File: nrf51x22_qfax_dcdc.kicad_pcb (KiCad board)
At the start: 2 copper layers, 14.8 x 16.4 mm, 46 parts, among them U1 nrf51822-qfax, X1 Crystal-4, X2 32.768kHz

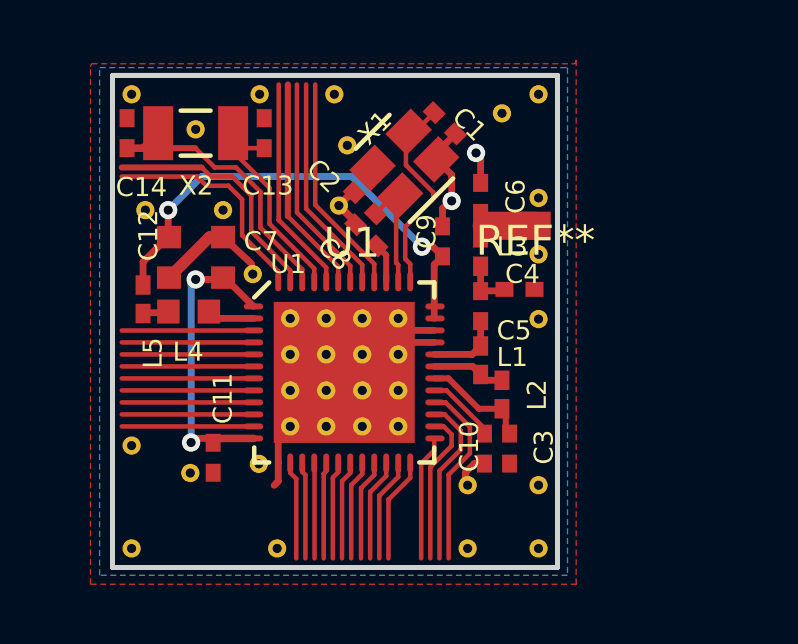
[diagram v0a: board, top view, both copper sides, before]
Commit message: converted qfaa dcdc reference layout .9
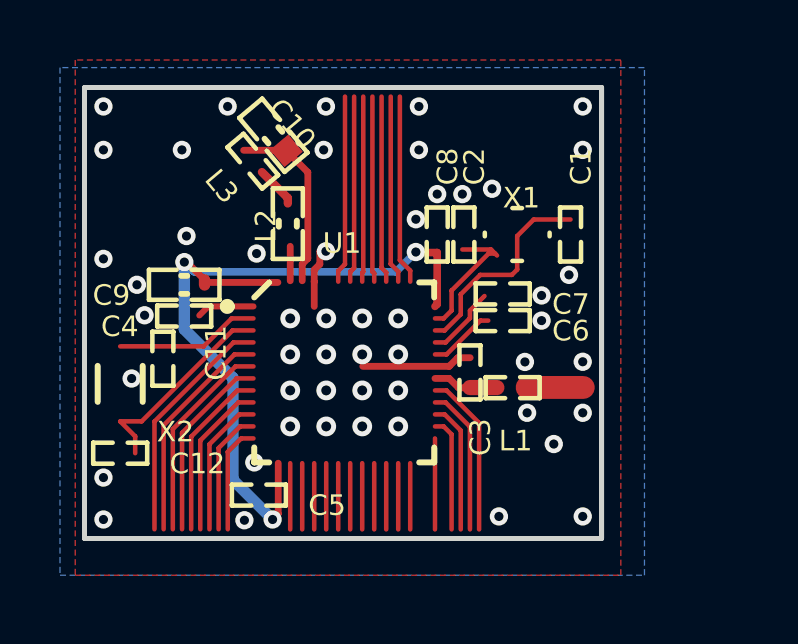
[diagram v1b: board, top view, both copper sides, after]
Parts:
- removed C1, C13, C14: 12pF, dcdc:CAPC1005X04L
- removed C10: 47nF, dcdc:CAPC1005X04L
- removed the C11 at (79.7, -82.6)
- removed the C12 at (78.3, -89.3)
- removed C3: 2.2nF, dcdc:CAPC1005X04L
- removed C4: 1.0pF, dcdc:CAPC1005X04L
- removed L1: 4.7nH, dcdc:INDC1005X04L
- removed L3: 3.3nH, dcdc:INDC1005X04L
- removed L4: 10uH, dcdc:INDC1608X06L
- removed REF** (x23): VIA-0.6096, dcdc:VIA-0.6096
- removed REF**: antenna, dcdc:antenna
- added C11: Chip Capacitor, 2-Leads, Body 1.6x0.8mm, IPC High Density, CAPC1608X06L, F.Cu at (81.7, -93.4)
- added C11: Chip Capacitor, 2-Leads, Body 1.0x0.5mm, IPC High Density, CAPC1005X04L, F.Cu at (89.4, -88.1)
- added C11: Chip Capacitor, 2-Leads, Body 1.0x0.5mm, IPC High Density, CAPC1005X04L, F.Cu at (78.1, -85.9)
- added C12: Chip Capacitor, 2-Leads, Body 1.0x0.5mm, IPC High Density, CAPC1005X04L, F.Cu at (87.2, -90.1)
- added C12: Chip Capacitor, 2-Leads, Body 1.0x0.5mm, IPC High Density, CAPC1005X04L, F.Cu at (76.6, -82.8)
- added C20: Chip Capacitor, 2-Leads, Body 1.0x0.5mm, IPC High Density, CAPC1005X04L, F.Cu at (88.3, -85.5)
- added L6: Chip Inductor, 2-Leads, Body 1.0x0.5mm, IPC High Density, INDC1005X04L, F.Cu at (81.1, -92.5)
- C2: value 12pF -> Chip Capacitor, 2-Leads, Body 1.0x0.5mm, IPC High Density; footprint dcdc:CAPC1005X04L -> CAPC1005X04L
- C5: value 3.9pF -> Chip Capacitor, 2-Leads, Body 1.0x0.5mm, IPC High Density; footprint dcdc:CAPC1005X04L -> CAPC1005X04L
- C6: value 1.5pF -> Chip Capacitor, 2-Leads, Body 1.0x0.5mm, IPC High Density; footprint dcdc:CAPC1005X04L -> CAPC1005X04L
- C7: value 4.7uF -> Chip Capacitor, 2-Leads, Body 1.0x0.5mm, IPC High Density; footprint dcdc:CAPC1608X06L -> CAPC1005X04L
- C8: value 100nF -> Chip Capacitor, 2-Leads, Body 1.0x0.5mm, IPC High Density; footprint dcdc:CAPC1005X04L -> CAPC1005X04L
- C9: value 1.0nF -> Chip Capacitor, 2-Leads, Body 1.6x0.8mm, IPC High Density; footprint dcdc:CAPC1005X04L -> CAPC1608X06L
- L2: value 27nH -> Chip Inductor, 2-Leads, Body 1.0x0.5mm, IPC High Density; footprint dcdc:INDC1005X04L -> INDC1005X04L
- L5: value 15nH -> Chip Inductor, 2-Leads, Body 1.6x0.8mm, IPC High Density; footprint dcdc:INDC1005X04L -> INDC1608X06L
- U1: value nrf51822-qfax -> QFN, 48-Leads, Body 6,0x6,0mm (max), Pitch 0,40mm, IPC Medium Density; footprint nrf:nrf51-qfax-1ep-vias -> QFN40P600X600X90-48N
- X1: value Crystal-4 -> Crystal 2.0 x 1.6 mm; footprint dcdc:BT-XTAL_2520 -> BT-XTAL_2016
- X2: value 32.768kHz -> XTAL SMD 3.2 x 1.5 mm; footprint dcdc:XTAL_3215 -> XTAL_3215
- moved C6 12.4 mm to (81.3, -81.4), turned to 0 degrees
- moved C7 11.6 mm to (91.6, -90.1)
- moved C5 9.89 mm to (78.8, -87.4), turned to 0 degrees
- moved C9 8.73 mm to (78.8, -88.4), turned to 0 degrees
- moved X2 8.73 mm to (76.6, -85.1), turned to 0 degrees
- moved L5 5.44 mm to (82.2, -90.4)
- moved C8 5.36 mm to (89.4, -87.2), turned to 0 degrees
- moved X1 4.44 mm to (89.9, -90.1), turned to 0 degrees
- moved C2 3.46 mm to (88.1, -90.1), turned to 0 degrees
- moved L2 0.42 mm to (89.7, -85.0)
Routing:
- net Net1: track 0.00 -> 302.1 mm
- net (no net): track 149.8 -> 0.00 mm
- net GND: track 19.3 -> 0.00 mm, vias 2 -> 51
- net Net-(C12-Pad1): track 15.7 -> 0.00 mm, vias 2 -> 0
- net Net-(C11-Pad1): track 11.2 -> 0.00 mm, vias 2 -> 0
- net Net-(C14-Pad2): track 9.89 -> 0.00 mm
- net Net-(C1-Pad1): track 6.86 -> 0.00 mm
- net Net-(C13-Pad2): track 6.04 -> 0.00 mm
- net Net-(C2-Pad1): track 4.00 -> 0.00 mm
- net Net-(C3-Pad1): track 3.56 -> 0.00 mm
- net Net-(C5-Pad2): track 2.52 -> 0.00 mm
- net Net-(L1-Pad2): track 2.45 -> 0.00 mm
- net Net-(C10-Pad2): track 2.37 -> 0.00 mm
- net Net-(C4-Pad1): track 1.69 -> 0.00 mm
- net Net-(C6-Pad1): track 1.63 -> 0.00 mm
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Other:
- board size 14.8 x 16.4 mm -> 17.2 x 15 mm
- net class Default: clearance 0.1524 -> 0.152400; trace_width 0.254 -> 0.254000; via_dia 0.6096 -> 0.889; via_drill 0.3048 -> 0.635
- net class Net-(C6-Pad1) removed
- rule trace_clearance: 0.1524 -> 0.127
- rule trace_min: 0.152 -> 0.254
- rule via_min_drill: 0.3048 -> 0.508
- rule via_min_size: 0.6096 -> 0.889
- board text removed: "C13"
- board text removed: "C14"
- board text removed: "L4"
- board text removed: "L5"

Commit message: kicad touches and updats kicad_pcb
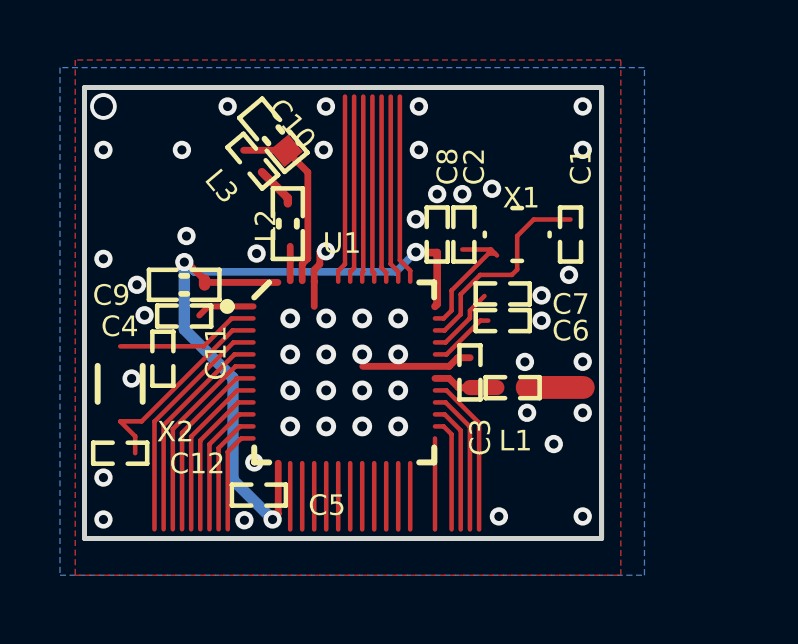
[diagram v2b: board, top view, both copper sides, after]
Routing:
- net Net1: track 302.1 -> 0.00 mm
- net (no net): track 0.00 -> 296.0 mm, vias 0 -> 54
- net DEC4: track 0.00 -> 6.11 mm
- net VDD_NRF: vias 3 -> 0
- net GND: vias 51 -> 0
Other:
- net class Default: clearance 0.152400 -> 0.1524; trace_width 0.254000 -> 0.254
- rule trace_clearance: 0.127 -> 0.1524

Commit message: swap for stiched vias
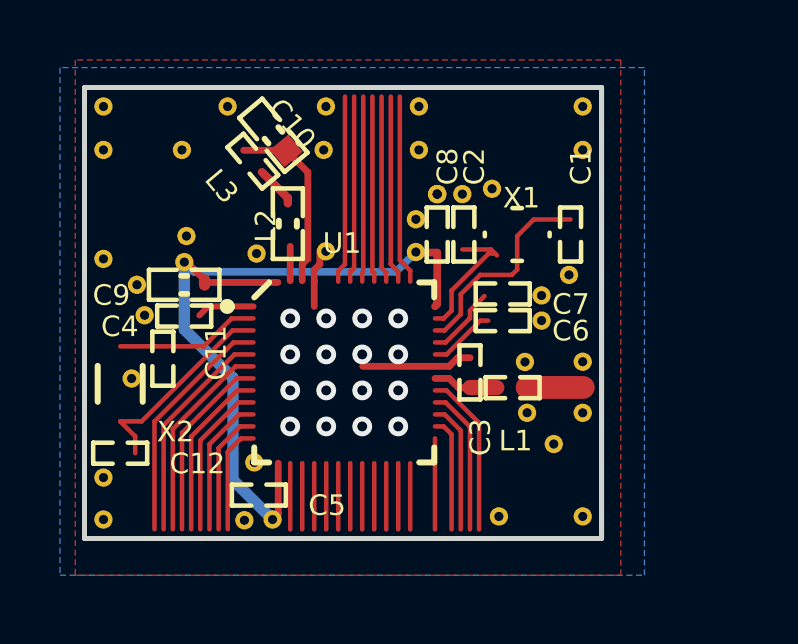
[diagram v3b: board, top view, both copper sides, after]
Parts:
- added REF**: VIA-0.6096, dcdc:VIA-0.6096, F.Cu at (92.1, -94.4)
- added REF**: VIA-0.6096, dcdc:VIA-0.6096, F.Cu at (92.1, -80.7)
- added REF**: VIA-0.6096, dcdc:VIA-0.6096, F.Cu at (89.3, -80.7)
- added REF**: VIA-0.6096, dcdc:VIA-0.6096, F.Cu at (92.1, -84.1)
- added REF**: VIA-0.6096, dcdc:VIA-0.6096, F.Cu at (90.2, -84.1)
- added REF**: VIA-0.6096, dcdc:VIA-0.6096, F.Cu at (92.1, -85.8)
- added REF**: VIA-0.6096, dcdc:VIA-0.6096, F.Cu at (91.6, -88.7)
- added REF**: VIA-0.6096, dcdc:VIA-0.6096, F.Cu at (89.0, -91.6)
- added REF**: VIA-0.6096, dcdc:VIA-0.6096, F.Cu at (92.1, -92.9)
- added REF**: VIA-0.6096, dcdc:VIA-0.6096, F.Cu at (86.5, -90.6)
- added REF**: VIA-0.6096, dcdc:VIA-0.6096, F.Cu at (88.0, -91.4)
- added REF**: VIA-0.6096, dcdc:VIA-0.6096, F.Cu at (86.6, -94.4)
- added REF** (x2): VIA-0.6096, dcdc:VIA-0.6096, F.Cu at (87.2, -91.4)
- added REF**: VIA-0.6096, dcdc:VIA-0.6096, F.Cu at (86.6, -92.9)
- added REF**: VIA-0.6096, dcdc:VIA-0.6096, F.Cu at (83.4, -92.9)
- added REF**: VIA-0.6096, dcdc:VIA-0.6096, F.Cu at (76.1, -89.3)
- added REF**: VIA-0.6096, dcdc:VIA-0.6096, F.Cu at (78.8, -90.0)
- added REF**: VIA-0.6096, dcdc:VIA-0.6096, F.Cu at (76.1, -92.9)
- added REF**: VIA-0.6096, dcdc:VIA-0.6096, F.Cu at (78.8, -89.2)
- added REF**: VIA-0.6096, dcdc:VIA-0.6096, F.Cu at (77.2, -88.4)
- added REF**: VIA-0.6096, dcdc:VIA-0.6096, F.Cu at (86.5, -89.5)
- added REF**: VIA-0.6096, dcdc:VIA-0.6096, F.Cu at (81.2, -89.5)
- added REF**: VIA-0.6096, dcdc:VIA-0.6096, F.Cu at (80.8, -80.6)
- added REF**: VIA-0.6096, dcdc:VIA-0.6096, F.Cu at (91.1, -83.1)
- added REF**: VIA-0.6096, dcdc:VIA-0.6096, F.Cu at (81.7, -80.6)
- added REF**: VIA-0.6096, dcdc:VIA-0.6096, F.Cu at (81.1, -82.5)
- added REF**: VIA-0.6096, dcdc:VIA-0.6096, F.Cu at (77.5, -87.4)
- added REF**: VIA-0.6096, dcdc:VIA-0.6096, F.Cu at (90.7, -87.2)
- added REF**: VIA-0.6096, dcdc:VIA-0.6096, F.Cu at (90.7, -88.1)
- added REF**: VIA-0.6096, dcdc:VIA-0.6096, F.Cu at (78.7, -92.9)
- added REF**: VIA-0.6096, dcdc:VIA-0.6096, F.Cu at (90.1, -85.8)
- added REF**: VIA-0.6096, dcdc:VIA-0.6096, F.Cu at (83.5, -89.5)
- added REF**: VIA-0.6096, dcdc:VIA-0.6096, F.Cu at (76.1, -94.4)
- added REF**: VIA-0.6096, dcdc:VIA-0.6096, F.Cu at (80.2, -94.4)
- added REF**: VIA-0.6096, dcdc:VIA-0.6096, F.Cu at (83.5, -94.4)
- added REF**: VIA-0.6096, dcdc:VIA-0.6096, F.Cu at (77.0, -85.3)
- added REF**: VIA-0.6096, dcdc:VIA-0.6096, F.Cu at (76.1, -82.0)
- added REF**: VIA-0.6096, dcdc:VIA-0.6096, F.Cu at (76.1, -80.6)
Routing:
- net GND: track 0.00 -> 28.0 mm
- net (no net): track 296.0 -> 268.0 mm, vias 54 -> 16

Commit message: replace components with library parts
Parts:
- removed the C11 at (81.7, -93.4)
- removed the C11 at (89.4, -88.1)
- removed the C11 at (78.1, -85.9)
- removed the C12 at (87.2, -90.1)
- removed the C12 at (76.6, -82.8)
- removed C20: Chip Capacitor, 2-Leads, Body 1.0x0.5mm, IPC High Density, CAPC1005X04L
- removed L5: Chip Inductor, 2-Leads, Body 1.6x0.8mm, IPC High Density, INDC1608X06L
- removed L6: Chip Inductor, 2-Leads, Body 1.0x0.5mm, IPC High Density, INDC1005X04L
- removed the REF** at (87.2, -91.4) (x2)
- added C1: Chip Capacitor, 2-Leads, Body 1.0x0.5mm, IPC High Density, dcdc:CAPC1005X04L, F.Cu at (91.6, -90.1)
- added C10: Chip Capacitor, 2-Leads, Body 1.6x0.8mm, IPC High Density, dcdc:CAPC1608X06L, F.Cu at (81.7, -93.4)
- added C11: Chip Capacitor, 2-Leads, Body 1.0x0.5mm, IPC High Density, dcdc:CAPC1005X04L, F.Cu at (78.1, -85.9)
- added C12: Chip Capacitor, 2-Leads, Body 1.0x0.5mm, IPC High Density, dcdc:CAPC1005X04L, F.Cu at (76.6, -82.8)
- added C3: Chip Capacitor, 2-Leads, Body 1.0x0.5mm, IPC High Density, dcdc:CAPC1005X04L, F.Cu at (88.3, -85.5)
- added C4: Chip Capacitor, 2-Leads, Body 1.0x0.5mm, IPC High Density, dcdc:CAPC1005X04L, F.Cu at (78.8, -87.4)
- added L1: Chip Inductor, 2-Leads, Body 1.0x0.5mm, IPC High Density, dcdc:INDC1005X04L, F.Cu at (89.7, -85.0)
- added L3: Chip Inductor, 2-Leads, Body 1.0x0.5mm, IPC High Density, dcdc:INDC1005X04L, F.Cu at (81.1, -92.5)
- added REF** (x2): VIA-0.6096, dcdc:VIA-0.6096, F.Cu at (87.2, -91.4)
- C2, C5, C6, C7, C8: footprint CAPC1005X04L -> dcdc:CAPC1005X04L
- C9: footprint CAPC1608X06L -> dcdc:CAPC1608X06L
- L2: value Chip Inductor, 2-Leads, Body 1.0x0.5mm, IPC High Density -> Chip Inductor, 2-Leads, Body 1.6x0.8mm, IPC High Density; footprint INDC1005X04L -> dcdc:INDC1608X06L
- U1: footprint QFN40P600X600X90-48N -> nrf:nrf51-qfax-1ep-vias
- X2: footprint XTAL_3215 -> dcdc:XTAL_3215
- moved C6 9.99 mm to (89.4, -87.2)
- moved L2 9.27 mm to (82.2, -90.4), turned to 90 degrees
- moved C5 6.47 mm to (81.3, -81.4)
- moved C8 3.61 mm to (87.2, -90.1), turned to 90 degrees
- moved C7 3.01 mm to (89.4, -88.1)
- turned C2 to 90 degrees
- turned C9 to 90 degrees
- turned X2 to 90 degrees
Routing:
- net (no net): track 268.0 -> 274.1 mm, vias 16 -> 0
- net DEC4: track 6.11 -> 0.00 mm

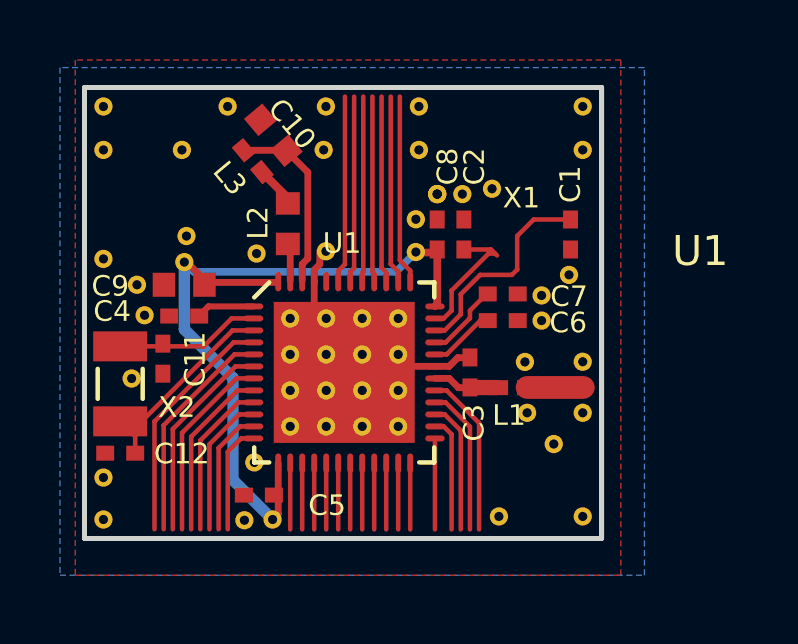
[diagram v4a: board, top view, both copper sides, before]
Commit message: fix zones and pour
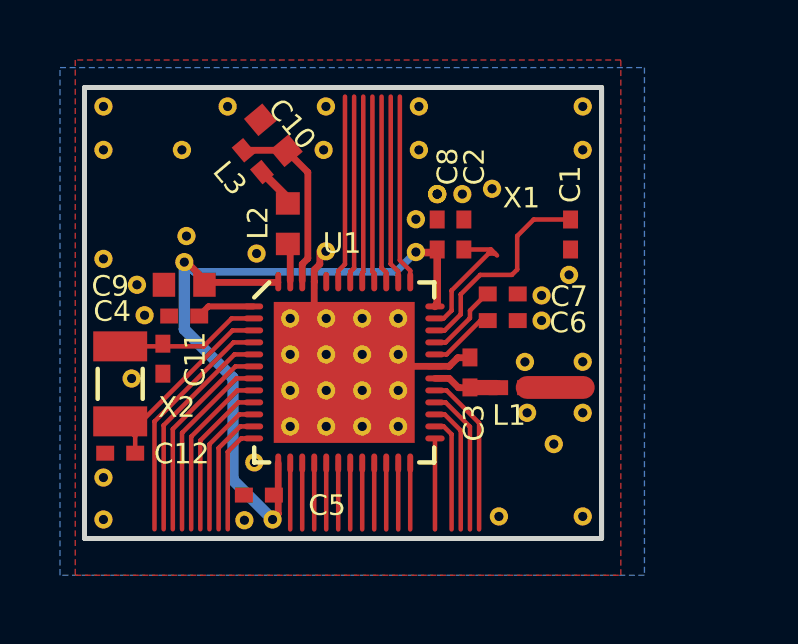
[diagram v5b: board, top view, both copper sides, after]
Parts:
- removed the REF** at (87.2, -91.4) (x2)
- added REF** (x2): VIA-0.6096, dcdc:VIA-0.6096, F.Cu at (87.2, -91.4)
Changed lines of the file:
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@@
   (general
     (links 38)
-    (no_connects 35)
+    (no_connects 0)
     (area 40.900936 -125.826416 125.126534 -49.754218)
     (thickness 1.6)
@@
     (last_trace_width 0.254)
     (trace_clearance 0.1524)
-    (zone_clearance 0.0144)
-    (zone_45_only no)
+    (zone_clearance 0.09144)
+    (zone_45_only yes)
     (trace_min 0.254)
     (segment_width 0.2)
@@
     (tags "QFN 0.4")
     (attr smd)
-    (fp_text reference U1 (at 11.867965 -4.043383) (layer F.SilkS)
+    (fp_text reference U1 (at 11.867965 -4.043383) (layer F.SilkS) hide
       (effects (font (size 1 1) (thickness 0.15)))
     )
@@
   (zone (net 2) (net_name GND) (layer F.Cu) (hatch edge 0.508)
     (priority 100)
-    (connect_pads thru_hole_only (clearance 0.09144))
+    (connect_pads (clearance 0.09144))
     (min_thickness 0.254)
-    (fill (mode segment) (arc_segments 32) (thermal_gap 0.254) (thermal_bridge_width 0.254))
+    (fill yes (arc_segments 32) (thermal_gap 0.254) (thermal_bridge_width 0.255))
     (polygon
       (pts
@@
   (zone (net 2) (net_name GND) (layer B.Cu) (hatch edge 0.508)
     (priority 99)
-    (connect_pads thru_hole_only (clearance 0.09144))
+    (connect_pads (clearance 0.09144))
     (min_thickness 0.254)
-    (fill (mode segment) (arc_segments 32) (thermal_gap 0.254) (thermal_bridge_width 0.254))
+    (fill yes (arc_segments 32) (thermal_gap 0.254) (thermal_bridge_width 0.255))
     (polygon
       (pts
-        (xy 74.631735 -95.651625) (xy 74.631735 -78.730462) (xy 94.113535 -78.730462) (xy 94.113535 -95.651625) (xy 74.631735 -95.651625)
+        (xy 94.113535 -78.730462) (xy 74.631735 -78.730462) (xy 74.631735 -95.651625) (xy 94.113535 -95.651625) (xy 94.113535 -78.730462)
       )
     )
+  )
+  (zone (net 0) (net_name "") (layer F.Cu) (hatch edge 0.508)
+    (connect_pads (clearance 0.09144))
+    (min_thickness 0.254)
+    (keepout (tracks allowed) (vias allowed) (copperpour not_allowed))
+    (fill (arc_segments 32) (thermal_gap 0.254) (thermal_bridge_width 0.255))
+    (polygon
+      (pts
+        (xy 89.7763 -83.7692) (xy 88.265 -83.7692) (xy 88.265 -86.6775) (xy 89.7763 -86.6775) (xy 89.7763 -83.7692)
+      )
+    )

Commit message: cleanup
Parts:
- removed the REF** at (87.2, -91.4) (x2)
- added REF** (x2): VIA-0.6096, dcdc:VIA-0.6096, F.Cu at (87.2, -91.4)

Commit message: schematic and netlist imported to board
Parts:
- removed the REF** at (87.2, -91.4) (x2)
- added REF** (x2): VIA-0.6096, dcdc:VIA-0.6096, F.Cu at (87.2, -91.4)
- C1, C11, C12, C2: value Chip Capacitor, 2-Leads, Body 1.0x0.5mm, IPC High Density -> 12pF
- C10: value Chip Capacitor, 2-Leads, Body 1.6x0.8mm, IPC High Density -> 1.0uF
- C3: value Chip Capacitor, 2-Leads, Body 1.0x0.5mm, IPC High Density -> .8pF
- C4, C5, C8: value Chip Capacitor, 2-Leads, Body 1.0x0.5mm, IPC High Density -> 100nF
- C6: value Chip Capacitor, 2-Leads, Body 1.0x0.5mm, IPC High Density -> NC
- C7: value Chip Capacitor, 2-Leads, Body 1.0x0.5mm, IPC High Density -> 100pF
- C9: value Chip Capacitor, 2-Leads, Body 1.6x0.8mm, IPC High Density -> 4.7uF
- L1: value Chip Inductor, 2-Leads, Body 1.0x0.5mm, IPC High Density -> 3.9nH
- L2: value Chip Inductor, 2-Leads, Body 1.6x0.8mm, IPC High Density -> 10uH
- L3: value Chip Inductor, 2-Leads, Body 1.0x0.5mm, IPC High Density -> 15nH
- U1: value QFN, 48-Leads, Body 6,0x6,0mm (max), Pitch 0,40mm, IPC Medium Density -> nrf51822-qfax
- X1: value Crystal 2.0 x 1.6 mm -> Crystal-4
- X2: value XTAL SMD 3.2 x 1.5 mm -> 32.768kHz
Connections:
- C1 pad 1: (no net) -> Net-(C1-Pad1)
- C1 pad 2: (no net) -> GND
- C10 pad 1: (no net) -> GND
- C10 pad 2: DEC4 -> Net-(C10-Pad2)
- C11 pad 1: (no net) -> GND
- C11 pad 2: (no net) -> Net-(C11-Pad2)
- C12 pad 1: (no net) -> GND
- C12 pad 2: (no net) -> Net-(C12-Pad2)
- C2 pad 1: (no net) -> Net-(C2-Pad1)
- C2 pad 2: (no net) -> GND
- C3 pad 1: (no net) -> Net-(C3-Pad1)
- C3 pad 2: (no net) -> GND
- C4 pad 1: (no net) -> GND
- C4 pad 2: (no net) -> Net-(C4-Pad2)
- C5 pad 1: (no net) -> GND
- C5 pad 2: (no net) -> /VDD_nRF
- C6 pad 1: (no net) -> GND
- C6 pad 2: (no net) -> Net-(C6-Pad2)
- C7 pad 1: (no net) -> GND
- C7 pad 2: (no net) -> Net-(C7-Pad2)
- C8 pad 1: (no net) -> GND
- C8 pad 2: (no net) -> /VDD_nRF
- C9 pad 1: (no net) -> GND
- C9 pad 2: (no net) -> /VDD_nRF
- L1 pad 1: (no net) -> Net-(C3-Pad1)
- L2 pad 1: (no net) -> Net-(L2-Pad1)
- L2 pad 2: (no net) -> Net-(L2-Pad2)
- L3 pad 1: (no net) -> Net-(C10-Pad2)
- L3 pad 2: (no net) -> Net-(L2-Pad1)
- U1 pad 1: (no net) -> Net-(C4-Pad2)
- U1 pad 13: (no net) -> /VDD_nRF
- U1 pad 2: (no net) -> Net-(C11-Pad2)
- U1 pad 3: (no net) -> Net-(C12-Pad2)
- U1 pad 30: (no net) -> Net-(C3-Pad1)
- U1 pad 31: (no net) -> GND
- U1 pad 32: (no net) -> Net-(C6-Pad2)
- U1 pad 33: (no net) -> Net-(C7-Pad2)
- U1 pad 34: (no net) -> Net-(C1-Pad1)
- U1 pad 35: (no net) -> Net-(C2-Pad1)
- U1 pad 36: (no net) -> /VDD_nRF
- U1 pad 45: (no net) -> GND
- U1 pad 46: (no net) -> Net-(C10-Pad2)
- U1 pad 47: (no net) -> Net-(L2-Pad2)
- U1 pad 48: (no net) -> /VDD_nRF
- U1 pad 49: (no net) -> GND
- X2 pad 1: (no net) -> Net-(C12-Pad2)
- X2 pad 2: (no net) -> Net-(C11-Pad2)
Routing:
- net (no net): track 274.1 -> 229.5 mm
- net GND: track 28.0 -> 38.4 mm
- net Net-(C1-Pad1): track 0.00 -> 7.10 mm
- net Net-(C12-Pad2): track 0.00 -> 6.97 mm
- net Net-(C11-Pad2): track 0.00 -> 4.83 mm
- net Net-(C2-Pad1): track 0.00 -> 4.53 mm
- net Net-(L2-Pad1): track 0.00 -> 2.56 mm
- net Net-(C3-Pad1): track 0.00 -> 2.20 mm
- net /VDD_nRF: track 0.00 -> 1.83 mm
- net Net-(C10-Pad2): track 0.00 -> 1.77 mm
- net Net-(C4-Pad2): track 0.00 -> 1.50 mm

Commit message: no idea
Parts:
- removed the REF** at (87.2, -91.4) (x2)
- added REF** (x2): VIA-0.6096, dcdc:VIA-0.6096, F.Cu at (87.2, -91.4)
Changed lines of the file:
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@@
     (links 89)
     (no_connects 20)
-    (area 75.368339 -95.067421 92.766941 -79.878219)
+    (area 71.518807 -97.97362 97.2013 -77.09662)
     (thickness 1.6)
     (drawings 26)
